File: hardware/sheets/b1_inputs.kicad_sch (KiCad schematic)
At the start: 38 parts, among them U101 ADS8688IDBTR

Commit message: hardware: chip resistors and ceramic capacitors on KiCad standard footprints (Decision #47); schematic, library and gapped copies regenerated, ERC 0 errors
Co-Authored-By: Claude Fable 5.1 <noreply@anthropic.com>
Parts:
- C101, C103, C104, C108, C111, C112, C113, C114, C115, C116, C117, C118: footprint class_board:C0603 -> Capacitor_SMD:C_0603_1608Metric
- C102, C106, C107: footprint class_board:C0805 -> Capacitor_SMD:C_0805_2012Metric
- C105: footprint class_board:C1206 -> Capacitor_SMD:C_1206_3216Metric
- R101, R102, R111, R112, R113, R114, R115, R116, R117, R118: footprint class_board:R0603 -> Resistor_SMD:R_0603_1608Metric

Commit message: Schematic spacing rework: all nine sheets checker-clean, netlist fixes (LM66100 inputs off GND, TCXO divider joined), arrow rails, A2 for b5/c_switch/nmr_tx/nmr_rx; sch_check.py + net_diff.py; renders in docs/sch
Co-Authored-By: Claude Fable 5.1 <noreply@anthropic.com>
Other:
- moved on the sheet: C101, C102, C103, C104, C105, C106, C107, C108, C111, C112, C113, C114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

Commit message: Boards as hand-reworked by the instructor 2026-09-18 (Decision #66): three 2x20 links re-placed, jumpers -> headers, TCXO removed, 16 SMA; layout and routing in progress; review in the course repo notes
Co-Authored-By: Claude Fable 5.1 <noreply@anthropic.com>
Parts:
- added J6: Panel link 2x20 female, Connector_PinSocket_2.54mm:PinSocket_2x20_P2.54mm_Vertical, symbol class_board:HDR_2x20_FEMALE
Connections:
- net AGND: now also J6.1, J6.11, J6.13, J6.15, J6.17, J6.19, J6.21, J6.23, J6.25, J6.27, J6.29, J6.3, J6.31, J6.33, J6.35, J6.37, J6.39, J6.5, J6.7, J6.9
- net AI1: now also J6.40
- net AI2: now also J6.38
- net AI3: now also J6.36
- net AI4: now also J6.34
- net AI5: now also J6.30
- net AI6: now also J6.28
- net AI7: now also J6.26
- net AI8: now also J6.24
- net AIN1: now also U101.18 (AIN_1P); no longer U101.12 (AIN_6P)
- net AIN2: now also U101.16 (AIN_0P); no longer U101.14 (AIN_7P)
- net AIN3: now also U101.14 (AIN_7P); no longer U101.16 (AIN_0P)
- net AIN4: now also U101.12 (AIN_6P); no longer U101.18 (AIN_1P)
- net AIN5: now also U101.27 (AIN_5P); no longer U101.21 (AIN_2P)
- net AIN6: now also U101.25 (AIN_4P); no longer U101.23 (AIN_3P)
- net AIN7: now also U101.23 (AIN_3P); no longer U101.25 (AIN_4P)
- net AIN8: now also U101.21 (AIN_2P); no longer U101.27 (AIN_5P)
- new net AO1: J6.18
- new net AO2: J6.16
- new net AUX: J6.12
- new net RX: J6.32
- new net TX: J6.20, J6.22
- no-connect marks 1 -> 7
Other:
- note added: "1-6"
- note added: "13-18"
- note added: "19-24"
- note added: "25-30"
- note added: "31-36"
- note added: "37-40"
- note added: "7-12"
- note added: "AI1 AGND AI2 AGND AI3 AGND"
- note added: "AI4 AGND AI5 AGND AI6 AGND"
- note added: "AI7 AGND AI8 AGND RX AGND"
- note added: "AO1 AGND AO2 AGND spare AGND"
- note added: "J6 - analog, at x = 12 mm on the bottom side"
- note added: "J6 pin table"
- note added: "Pins"
- note added: "Signals (odd = signal, even = its return)"
- note added: "TX AGND TX AGND AUX AGND"
- note added: "spare AGND spare AGND"
- note added: "spare AGND spare AGND spare AGND"
- moved on the sheet: C101, C102, C103, C104, C105, C106, C107, C108, C111, C112, C113, C114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

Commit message: WIP main board routing + schematic (instructor), 2026-09-21 05:04
Co-Authored-By: Claude Fable 5.1 <noreply@anthropic.com>
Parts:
- removed JP101, JP102: SolderJumper_3_Bridged12, class_board:SolderJumper-3_P1.3mm_Bridged12_RoundedPad1.0x1.5mm, symbol class_board:SolderJumper_3_Bridged12
- added J14, J15: C2937625_-_Conn_01x03, DDS_Library:C2937625-HDR-TH_3P-P2.54-V-M, symbol DDS_Library:C2937625_-_Conn_01x03
- TP101: value TP -> AGND
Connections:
- net AI7: now also J14.1 (Pin_1)
- net AI8: now also J15.1 (Pin_1)
- net COND_OUT1: now also J14.3 (Pin_3)
- net COND_OUT2: now also J15.3 (Pin_3)
- net at R118.1: now also J15.2 (Pin_2)
- net at R117.1: now also J14.2 (Pin_2)

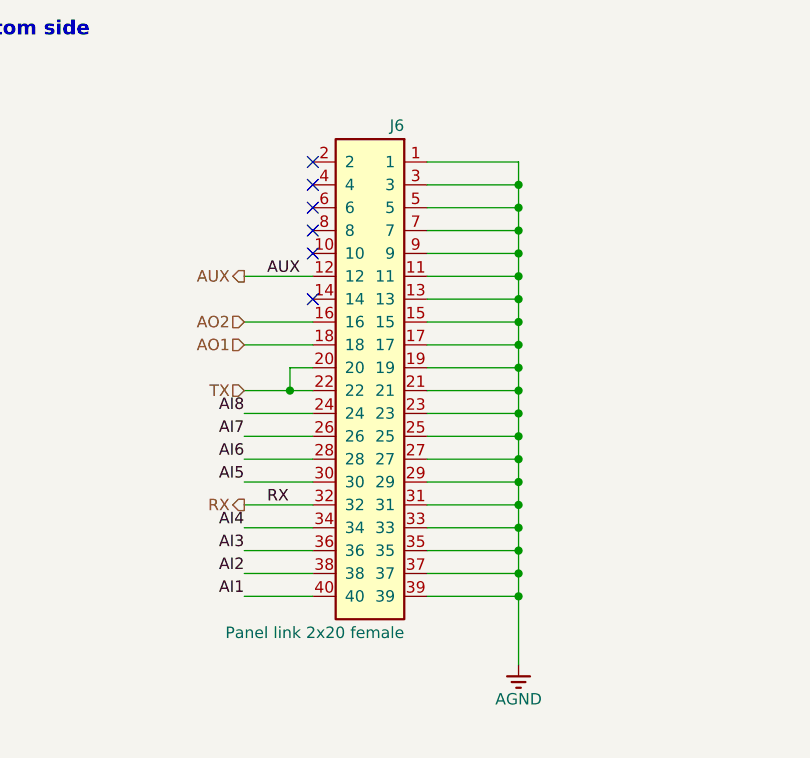
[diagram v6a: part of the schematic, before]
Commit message: hardware: b1_inputs sheet from the instructor's 2026-09-25 save
Co-Authored-By: Claude Fable 5.1 <noreply@anthropic.com>
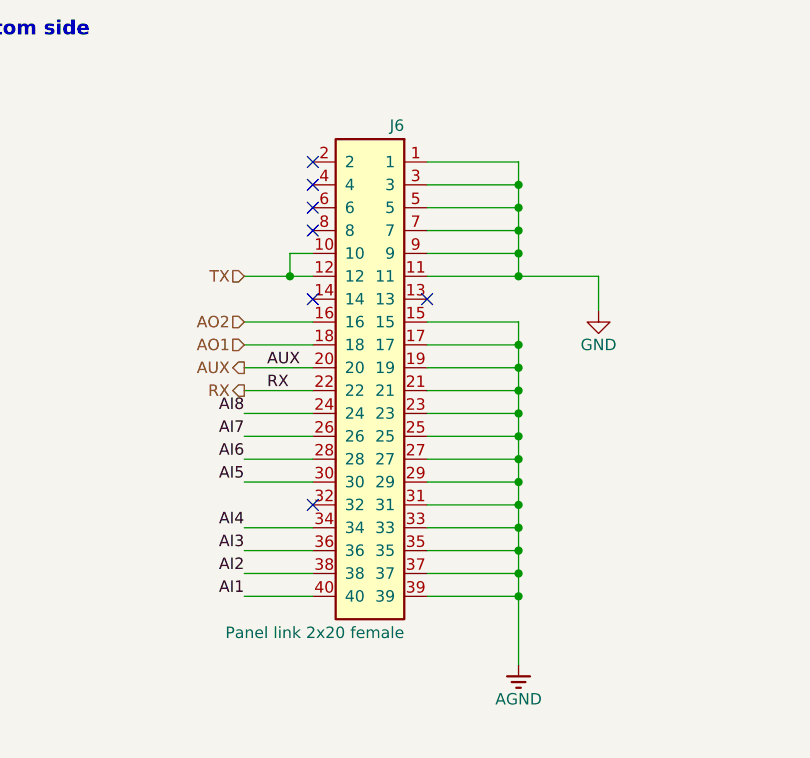
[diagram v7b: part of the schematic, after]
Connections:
- net AGND: no longer J6.1, J6.11, J6.13, J6.3, J6.5, J6.7, J6.9
- net AUX: now also J6.20; no longer J6.12
- net GND: now also J6.1, J6.11, J6.3, J6.5, J6.7, J6.9
- net RX: now also J6.22; no longer J6.32
- net TX: now also J6.10, J6.12; no longer J6.20, J6.22
- no-connect marks 7 -> 8

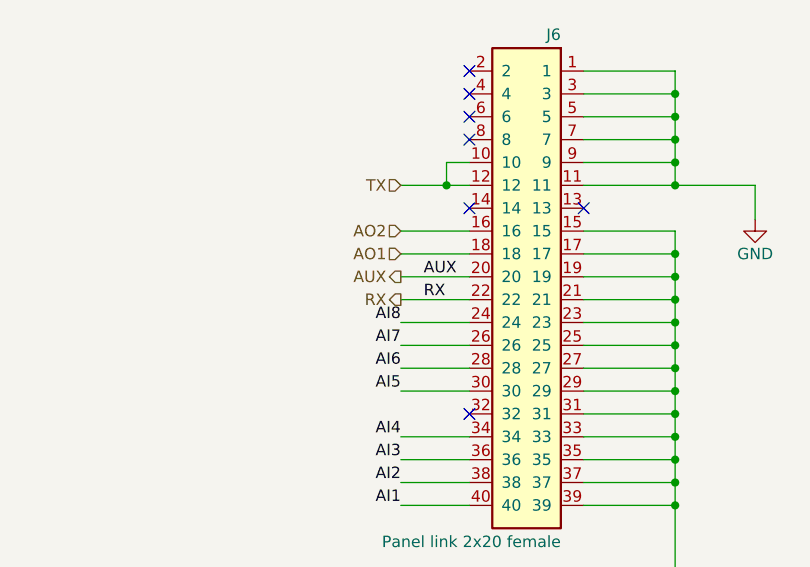
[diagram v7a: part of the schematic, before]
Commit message: Schematic review fixes, part 1 (branch, not merged): root sheet RX/AUX un-crossed + b1_inputs J6 pin 20/22 labels swapped (copper unchanged); firmware: ADC channel table kAinOfAi, FAST_OUT pins, module outputs 1-7 (relay -> module per PROTOCOL.md), AD9834 PIN/SW = 0, opto INPUT_PULLUP, stale comments; both PlatformIO envs build
Co-Authored-By: Claude Fable 5.1 <noreply@anthropic.com>
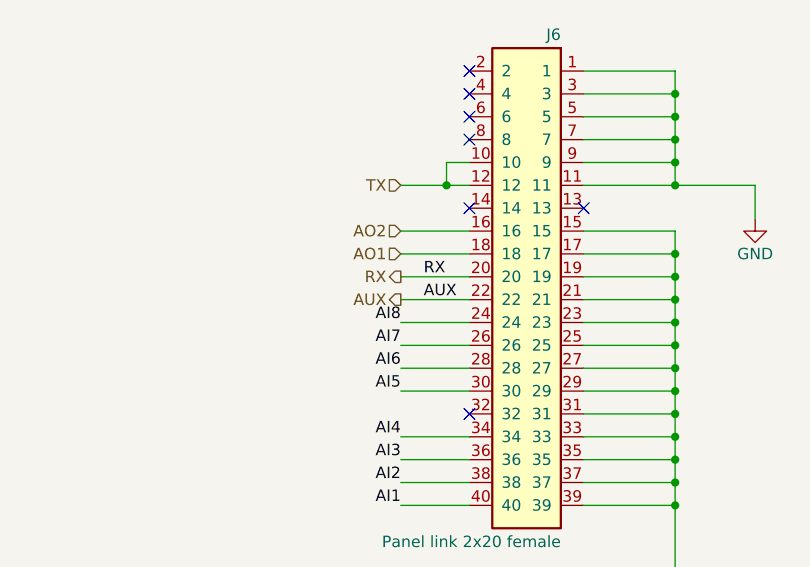
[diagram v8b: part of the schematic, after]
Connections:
- net AUX: now also J6.22; no longer J6.20
- net RX: now also J6.20; no longer J6.22
